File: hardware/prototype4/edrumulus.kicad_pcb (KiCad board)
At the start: 2 copper layers, 65 x 56.5 mm, 67 parts, among them J1 Trigger Connector, J2 Raspberry Pi GPIO pins, U1 ESP32-DEVKIT-V1

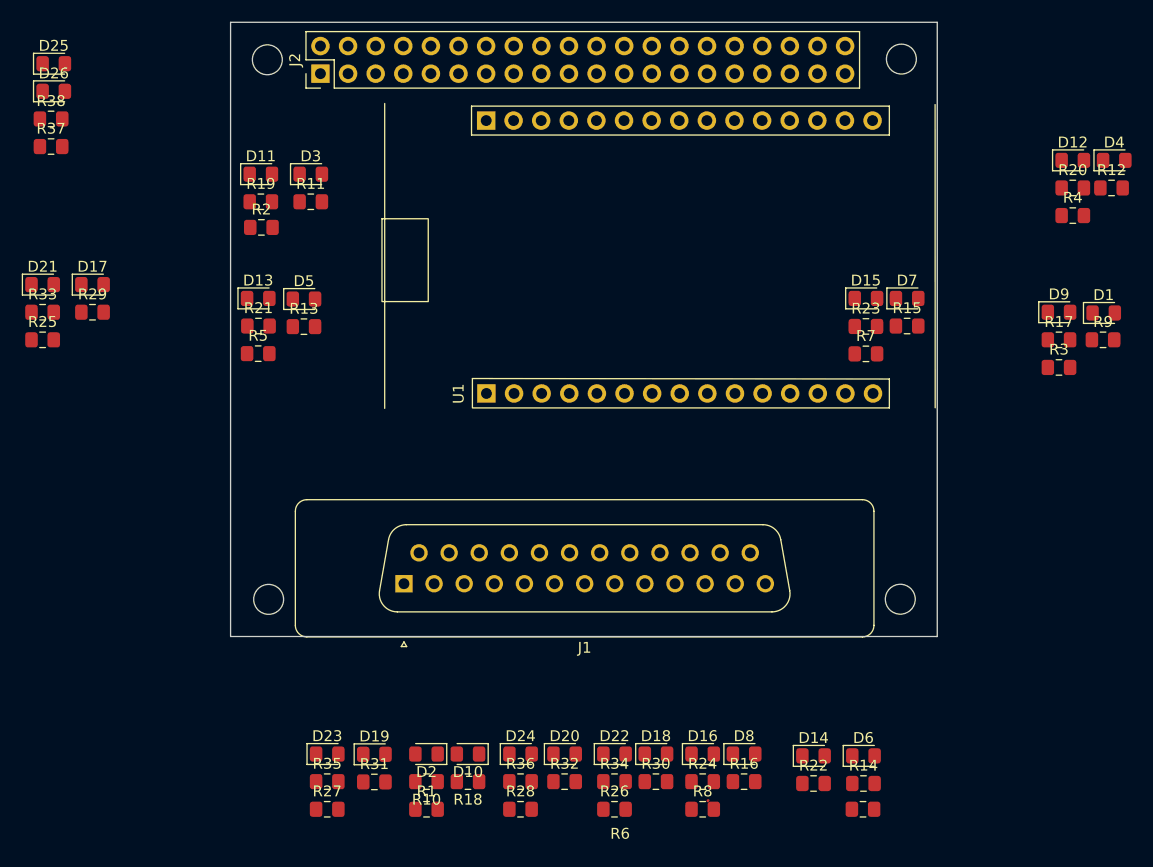
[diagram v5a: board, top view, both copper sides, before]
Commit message: diodes must have larger size on PCB
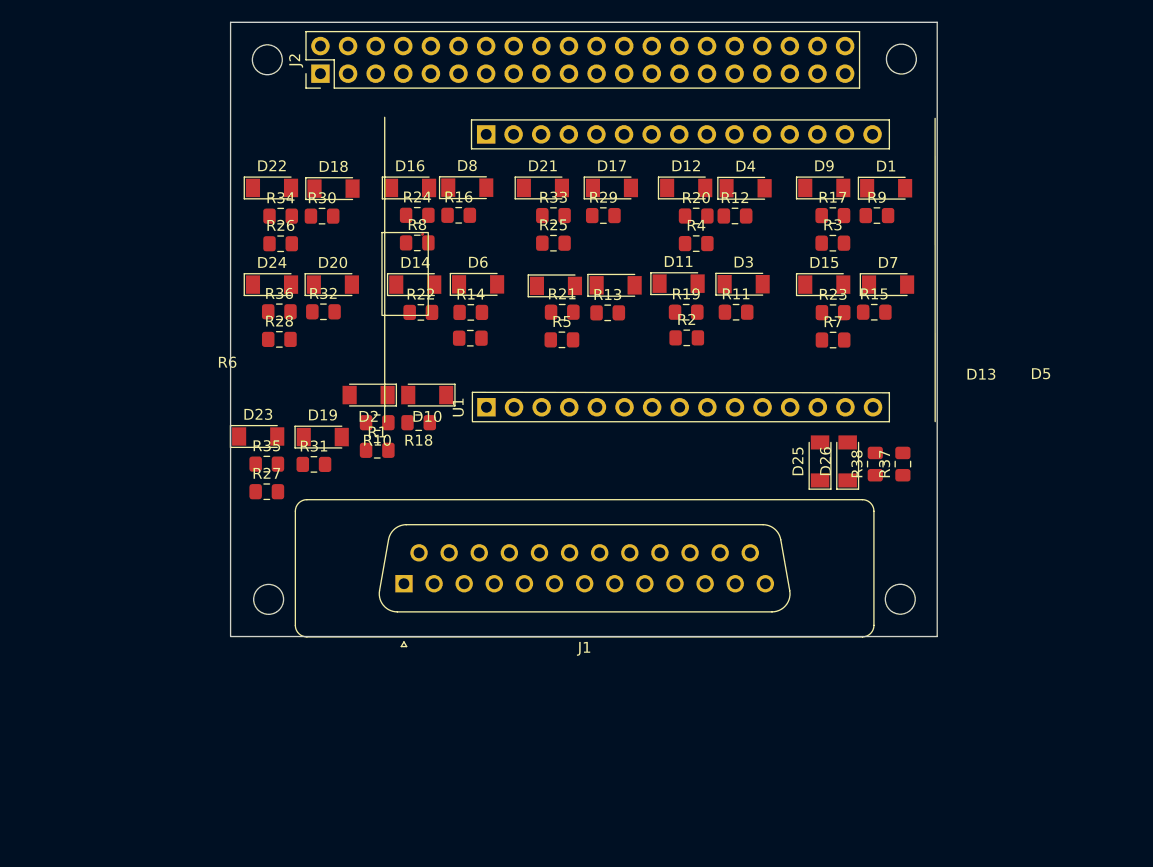
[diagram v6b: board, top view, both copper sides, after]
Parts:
- D1, D10, D11, D12, D13, D14, D15, D16, D17, D18, D19, D2, D20, D21, D22, D23, D24, D25, D26, D3, D4, D5, D6, D7, D8, D9: footprint Diode_SMD:D_0805_2012Metric_Pad1.15x1.40mm_HandSolder -> Diode_SMD:D_MiniMELF
- moved R37 83.6 mm to (168.5, 114.3), turned to 90 degrees
- moved R38 82.2 mm to (166.0, 114.3), turned to 90 degrees
- moved D26 80.6 mm to (163.4, 114.1), turned to 90 degrees
- moved D25 79.4 mm to (160.9, 114.1), turned to 90 degrees
- moved D22 60.9 mm to (110.5, 88.9)
- moved R26 60.4 mm to (111.3, 94.0)
- moved R30 60.4 mm to (115.1, 91.5)
- moved R34 60.4 mm to (111.3, 91.5)
- moved D18 59.9 mm to (116.1, 89.0)
- moved D16 58.6 mm to (123.2, 88.9)
- moved R8 58.3 mm to (123.9, 94.0)
- moved R16 58.3 mm to (127.7, 91.4)
- moved R24 58.3 mm to (123.9, 91.4)
- moved D8 58.0 mm to (128.5, 88.9)
- moved D14 56.8 mm to (123.7, 97.8)
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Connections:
- J1 pad 15: Net-(J1-Pad15) -> unconnected-(J1-Pad15)
- J1 pad 18: Net-(J1-Pad18) -> unconnected-(J1-Pad18)
- J1 pad 21: Net-(J1-Pad21) -> unconnected-(J1-Pad21)
- J1 pad 25: Net-(J1-Pad25) -> unconnected-(J1-Pad25)
- J2 pad 1: Net-(J2-Pad1) -> unconnected-(J2-Pad1)
- J2 pad 11: Net-(J2-Pad11) -> unconnected-(J2-Pad11)
- J2 pad 12: Net-(J2-Pad12) -> unconnected-(J2-Pad12)
- J2 pad 13: Net-(J2-Pad13) -> unconnected-(J2-Pad13)
- J2 pad 15: Net-(J2-Pad15) -> unconnected-(J2-Pad15)
- J2 pad 16: Net-(J2-Pad16) -> unconnected-(J2-Pad16)
- J2 pad 17: Net-(J2-Pad17) -> unconnected-(J2-Pad17)
- J2 pad 18: Net-(J2-Pad18) -> unconnected-(J2-Pad18)
- J2 pad 19: Net-(J2-Pad19) -> unconnected-(J2-Pad19)
- J2 pad 21: Net-(J2-Pad21) -> unconnected-(J2-Pad21)
- J2 pad 22: Net-(J2-Pad22) -> unconnected-(J2-Pad22)
- J2 pad 23: Net-(J2-Pad23) -> unconnected-(J2-Pad23)
- J2 pad 24: Net-(J2-Pad24) -> unconnected-(J2-Pad24)
- J2 pad 26: Net-(J2-Pad26) -> unconnected-(J2-Pad26)
- J2 pad 27: Net-(J2-Pad27) -> unconnected-(J2-Pad27)
- J2 pad 28: Net-(J2-Pad28) -> unconnected-(J2-Pad28)
- J2 pad 29: Net-(J2-Pad29) -> unconnected-(J2-Pad29)
- J2 pad 3: Net-(J2-Pad3) -> unconnected-(J2-Pad3)
- J2 pad 31: Net-(J2-Pad31) -> unconnected-(J2-Pad31)
- J2 pad 32: Net-(J2-Pad32) -> unconnected-(J2-Pad32)
- J2 pad 33: Net-(J2-Pad33) -> unconnected-(J2-Pad33)
- J2 pad 35: Net-(J2-Pad35) -> unconnected-(J2-Pad35)
- J2 pad 36: Net-(J2-Pad36) -> unconnected-(J2-Pad36)
- J2 pad 37: Net-(J2-Pad37) -> unconnected-(J2-Pad37)
- J2 pad 38: Net-(J2-Pad38) -> unconnected-(J2-Pad38)
- J2 pad 4: Net-(J2-Pad4) -> unconnected-(J2-Pad4)
- J2 pad 40: Net-(J2-Pad40) -> unconnected-(J2-Pad40)
- J2 pad 5: Net-(J2-Pad5) -> unconnected-(J2-Pad5)
- J2 pad 7: Net-(J2-Pad7) -> unconnected-(J2-Pad7)
- U1 pad 1: Net-(U1-Pad1) -> unconnected-(U1-Pad1)
- U1 pad 17: Net-(U1-Pad17) -> unconnected-(U1-Pad17)
- U1 pad 19: Net-(U1-Pad19) -> unconnected-(U1-Pad19)
- U1 pad 20: Net-(U1-Pad20) -> unconnected-(U1-Pad20)
- U1 pad 21: Net-(U1-Pad21) -> unconnected-(U1-Pad21)
- U1 pad 22: Net-(U1-Pad22) -> unconnected-(U1-Pad22)
- U1 pad 23: Net-(U1-Pad23) -> unconnected-(U1-Pad23)
- U1 pad 24: Net-(U1-Pad24) -> unconnected-(U1-Pad24)
- U1 pad 25: Net-(U1-Pad25) -> unconnected-(U1-Pad25)
- U1 pad 26: Net-(U1-Pad26) -> unconnected-(U1-Pad26)
- U1 pad 29: Net-(U1-Pad29) -> unconnected-(U1-Pad29)
- U1 pad 30: Net-(U1-Pad30) -> unconnected-(U1-Pad30)

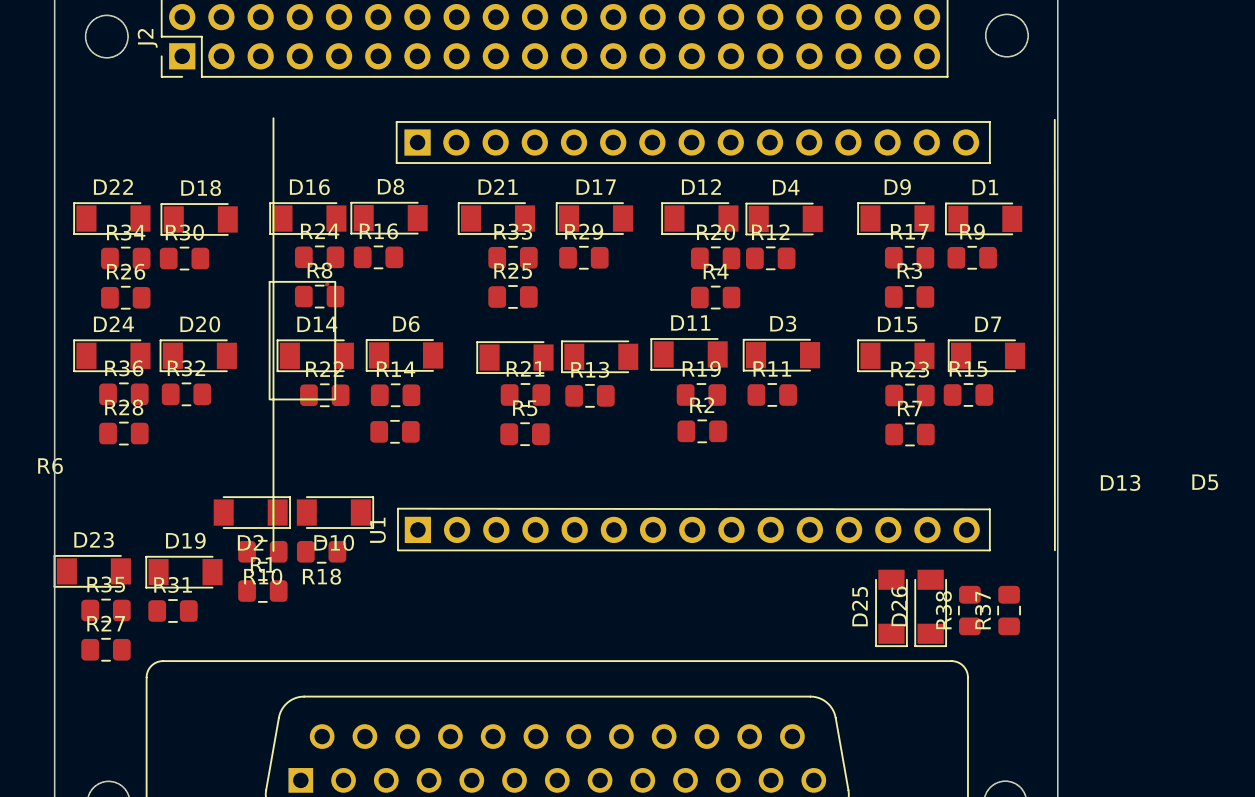
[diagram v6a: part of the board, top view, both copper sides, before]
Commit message: some more component reordering for prototype 4
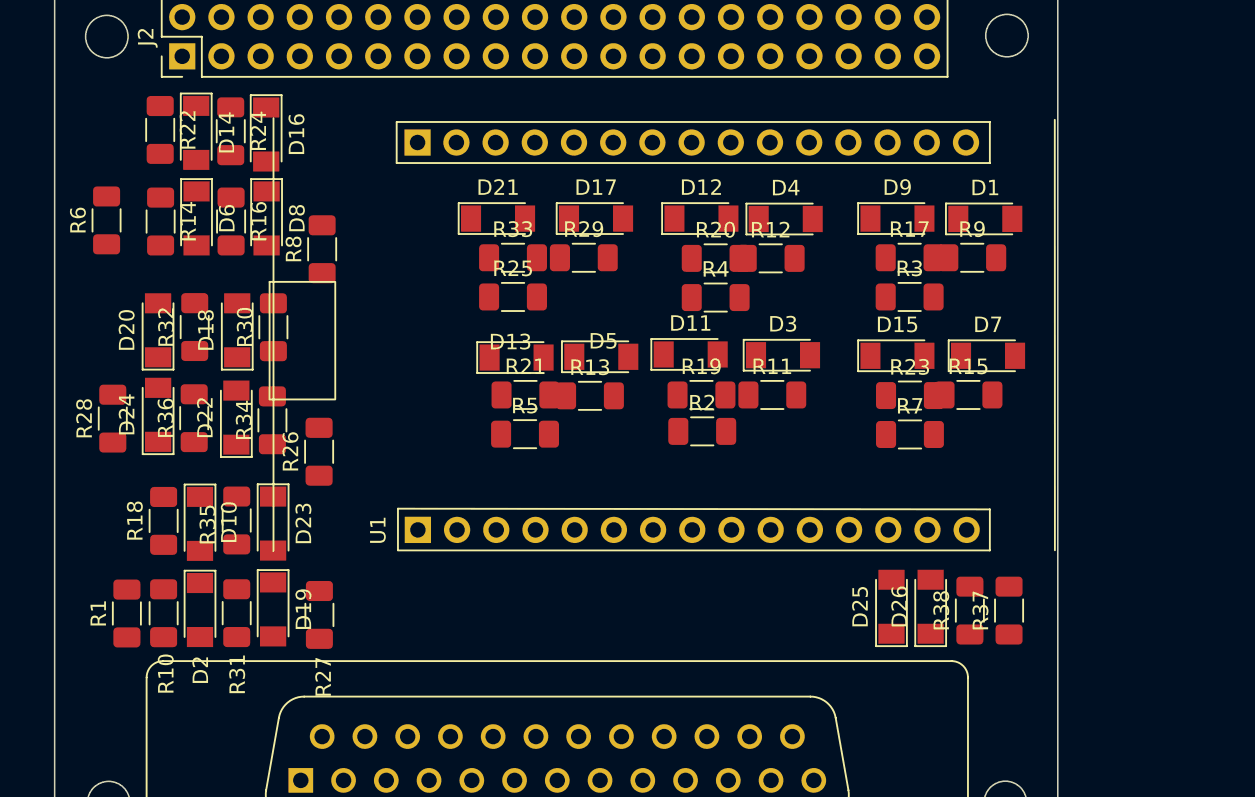
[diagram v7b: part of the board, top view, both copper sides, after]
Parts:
- R1, R10, R11, R12, R13, R14, R15, R16, R17, R18, R19, R2, R20, R21, R22, R23, R24, R25, R26, R27, R28, R29, R3, R30, R31, R32, R33, R34, R35, R36, R37, R38, R4, R5, R6, R7, R8, R9: footprint Resistor_SMD:R_0805_2012Metric_Pad1.15x1.40mm_HandSolder -> Resistor_SMD:R_1206_3216Metric_Pad1.30x1.75mm_HandSolder
- moved R6 23.2 mm to (110.0, 89.0), turned to 90 degrees
- moved R22 20.2 mm to (113.5, 83.2), turned to -90 degrees
- moved R14 18.9 mm to (113.5, 89.1), turned to -90 degrees
- moved D14 16.4 mm to (115.9, 83.3), turned to -90 degrees
- moved D6 16.2 mm to (115.9, 88.9), turned to -90 degrees
- moved R26 16.0 mm to (123.8, 104.0), turned to 90 degrees
- moved D22 15.2 mm to (118.5, 101.8), turned to 90 degrees
- moved R34 14.1 mm to (120.8, 102.0), turned to 90 degrees
- moved R27 14.0 mm to (123.8, 114.6), turned to 90 degrees
- moved D23 12.0 mm to (120.8, 108.7), turned to -90 degrees
- moved R18 10.4 mm to (113.7, 108.5), turned to -90 degrees
- moved R35 10.3 mm to (118.5, 108.5), turned to -90 degrees
- moved R24 10.00 mm to (118.1, 83.2), turned to -90 degrees
- moved R16 9.83 mm to (118.1, 89.1), turned to -90 degrees
- moved R1 8.93 mm to (111.4, 114.5), turned to 90 degrees
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
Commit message: some more routing
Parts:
- moved D1 70.5 mm to (237.3, 83.8)
- moved D3 70.5 mm to (224.2, 92.7)
- moved D9 70.5 mm to (231.6, 83.8)
- moved R12 70.5 mm to (223.4, 86.4)
- moved R20 70.5 mm to (219.8, 86.4)
- moved R4 70.5 mm to (219.8, 88.9)
- moved R9 70.5 mm to (236.5, 86.4)
- moved D11 70.5 mm to (218.2, 92.6)
- moved D12 70.5 mm to (218.9, 83.8)
- moved D4 70.5 mm to (224.4, 83.8)
- moved R11 70.5 mm to (223.5, 95.2)
- moved R17 70.5 mm to (232.4, 86.4)
- moved R19 70.5 mm to (218.9, 95.2)
- moved R2 70.5 mm to (219.0, 97.6)
- moved R3 70.5 mm to (232.4, 88.9)
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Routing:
- net CRASH1-TIP: track 0.00 -> 64.3 mm
- net SNARE-TIP: track 0.00 -> 63.3 mm
- net RIDE-TIP: track 0.00 -> 51.2 mm
- net RIDE-RING: track 0.00 -> 49.6 mm
- net CRASH1-RING: track 0.00 -> 45.3 mm
- net KICK-TIP: track 0.00 -> 44.3 mm
- net TOM3-TIP: track 0.00 -> 30.3 mm
- net HI-HAT-CONTROL-TIP: track 0.00 -> 27.4 mm
- net TOM1-TIP: track 0.00 -> 23.8 mm
- net TOM2-TIP: track 0.00 -> 14.4 mm
